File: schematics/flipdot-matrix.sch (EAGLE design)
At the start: 42 parts

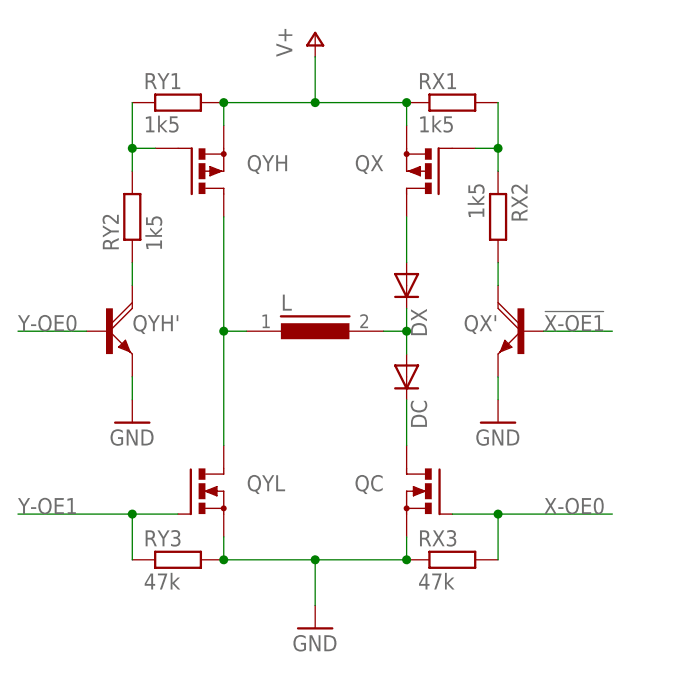
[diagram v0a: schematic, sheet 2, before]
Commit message: updated matrix schematics
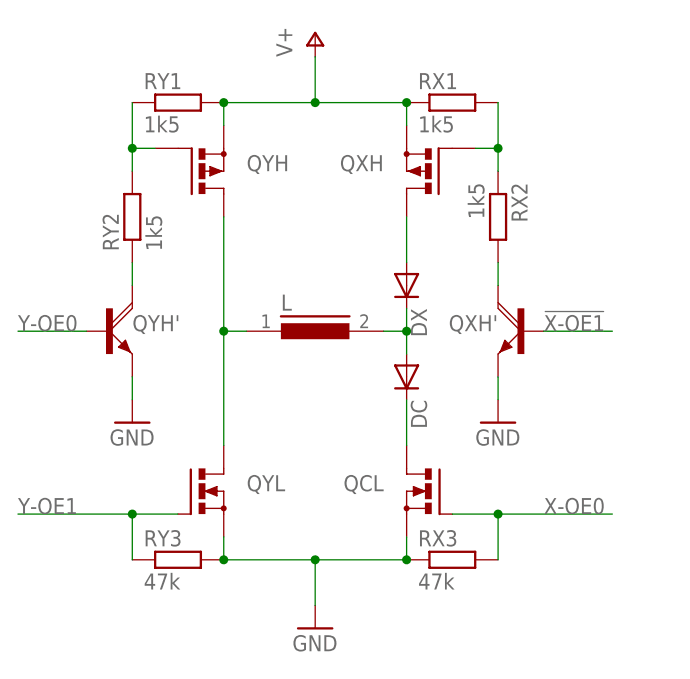
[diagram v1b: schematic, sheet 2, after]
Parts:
- renumbered QC to QCL, QX to QXH, QX' to QXH'
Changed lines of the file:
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@@
 <part name="L" library="inductors" deviceset="DS10" device="" value=""/>
 <part name="QYH" library="transistor-power" deviceset="PMOSFET_P" device="TO220BV"/>
-<part name="QX" library="transistor-power" deviceset="PMOSFET_P" device="TO220BV"/>
+<part name="QXH" library="transistor-power" deviceset="PMOSFET_P" device="TO220BV"/>
 <part name="QYL" library="transistor-power" deviceset="PMOSFET_N" device="TO220BV"/>
-<part name="QC" library="transistor-power" deviceset="PMOSFET_N" device="TO220BV"/>
+<part name="QCL" library="transistor-power" deviceset="PMOSFET_N" device="TO220BV"/>
 <part name="DC" library="diode" deviceset="1N4004" device="" value=""/>
 <part name="DX" library="diode" deviceset="1N4004" device="" value=""/>
@@
 <part name="P+2" library="supply1" deviceset="V+" device=""/>
 <part name="QYH'" library="transistor-power" deviceset="BD679" device="" value=""/>
-<part name="QX'" library="transistor-power" deviceset="BD679" device="" value=""/>
+<part name="QXH'" library="transistor-power" deviceset="BD679" device="" value=""/>
 <part name="GND1" library="supply1" deviceset="GND" device=""/>
 <part name="GND3" library="supply1" deviceset="GND" device=""/>
@@
 <sheets>
 <sheet>
-<description>Flip Dot Matrix</description>
+<description>Matrix</description>
 <plain>
 <rectangle x1="7.62" y1="50.8" x2="27.94" y2="71.12" layer="97"/>
@@
 </sheet>
 <sheet>
-<description>Flip Dot Pixel</description>
+<description>Pixel</description>
 <plain>
 </plain>
@@
 <attribute name="VALUE" x="25.4" y="53.34" size="1.778" layer="96"/>
 </instance>
-<instance part="QX" gate="G$1" x="45.72" y="53.34" smashed="yes" rot="MR0">
+<instance part="QXH" gate="G$1" x="45.72" y="53.34" smashed="yes" rot="MR0">
 <attribute name="NAME" x="40.64" y="53.34" size="1.778" layer="95" rot="MR0"/>
 <attribute name="VALUE" x="40.64" y="53.34" size="1.778" layer="96" rot="MR0"/>
@@
 <attribute name="VALUE" x="25.4" y="17.78" size="1.778" layer="96"/>
 </instance>
-<instance part="QC" gate="G$1" x="45.72" y="17.78" smashed="yes" rot="MR0">
+<instance part="QCL" gate="G$1" x="45.72" y="17.78" smashed="yes" rot="MR0">
 <attribute name="NAME" x="40.64" y="17.78" size="1.778" layer="95" rot="MR0"/>
 <attribute name="VALUE" x="40.64" y="17.78" size="1.778" layer="96" rot="MR0"/>
@@
 <attribute name="VALUE" x="15.24" y="35.56" size="1.778" layer="96"/>
 </instance>
-<instance part="QX'" gate="1" x="55.88" y="35.56" smashed="yes" rot="MR0">
+<instance part="QXH'" gate="1" x="55.88" y="35.56" smashed="yes" rot="MR0">
 <attribute name="NAME" x="53.34" y="35.56" size="1.778" layer="95" rot="MR0"/>
 <attribute name="VALUE" x="50.8" y="35.56" size="1.778" layer="96" rot="MR0"/>
@@
 <net name="N$24" class="0">
 <segment>
-<pinref part="QX" gate="G$1" pin="D"/>
+<pinref part="QXH" gate="G$1" pin="D"/>
 <pinref part="DX" gate="1" pin="A"/>
 <wire x1="43.18" y1="48.26" x2="43.18" y2="43.18" width="0.1524" layer="91"/>
@@
 <net name="N$26" class="0">
 <segment>
-<pinref part="QC" gate="G$1" pin="D"/>
+<pinref part="QCL" gate="G$1" pin="D"/>
 <pinref part="DC" gate="1" pin="C"/>
 <wire x1="43.18" y1="22.86" x2="43.18" y2="27.94" width="0.1524" layer="91"/>
@@
 <net name="X-OE0" class="0">
 <segment>
-<pinref part="QC" gate="G$1" pin="G"/>
+<pinref part="QCL" gate="G$1" pin="G"/>
 <wire x1="48.26" y1="15.24" x2="53.34" y2="15.24" width="0.1524" layer="91"/>
 <label x="58.42" y="15.24" size="1.778" layer="95"/>
@@
 <junction x="22.86" y="60.96"/>
 <pinref part="RX1" gate="G$1" pin="1"/>
-<pinref part="QX" gate="G$1" pin="S"/>
+<pinref part="QXH" gate="G$1" pin="S"/>
 <wire x1="43.18" y1="60.96" x2="43.18" y2="58.42" width="0.1524" layer="91"/>
 <junction x="43.18" y="60.96"/>
@@
 <wire x1="43.18" y1="10.16" x2="33.02" y2="10.16" width="0.1524" layer="91"/>
 <junction x="33.02" y="10.16"/>
-<pinref part="QC" gate="G$1" pin="S"/>
+<pinref part="QCL" gate="G$1" pin="S"/>
 <wire x1="43.18" y1="12.7" x2="43.18" y2="10.16" width="0.1524" layer="91"/>
 <junction x="43.18" y="10.16"/>
@@
 <segment>
 <pinref part="GND3" gate="1" pin="GND"/>
-<pinref part="QX'" gate="1" pin="E"/>
+<pinref part="QXH'" gate="1" pin="E"/>
 <wire x1="53.34" y1="30.48" x2="53.34" y2="27.94" width="0.1524" layer="91"/>
 </segment>
@@
 <net name="!X-OE1" class="0">
 <segment>
-<pinref part="QX'" gate="1" pin="B"/>
+<pinref part="QXH'" gate="1" pin="B"/>
 <wire x1="58.42" y1="35.56" x2="66.04" y2="35.56" width="0.1524" layer="91"/>
 <label x="58.42" y="35.56" size="1.778" layer="95"/>
@@
 <net name="N$11" class="0">
 <segment>
-<pinref part="QX'" gate="1" pin="C"/>
+<pinref part="QXH'" gate="1" pin="C"/>
 <pinref part="RX2" gate="G$1" pin="2"/>
 <wire x1="53.34" y1="40.64" x2="53.34" y2="43.18" width="0.1524" layer="91"/>
@@
 <pinref part="RX1" gate="G$1" pin="2"/>
 <wire x1="53.34" y1="53.34" x2="53.34" y2="55.88" width="0.1524" layer="91"/>
-<pinref part="QX" gate="G$1" pin="G"/>
+<pinref part="QXH" gate="G$1" pin="G"/>
 <wire x1="53.34" y1="55.88" x2="53.34" y2="60.96" width="0.1524" layer="91"/>
 <wire x1="50.8" y1="55.88" x2="53.34" y2="55.88" width="0.1524" layer="91"/>

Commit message: updated flipdot pixel: X-OE0 is inverted, not X-OE1
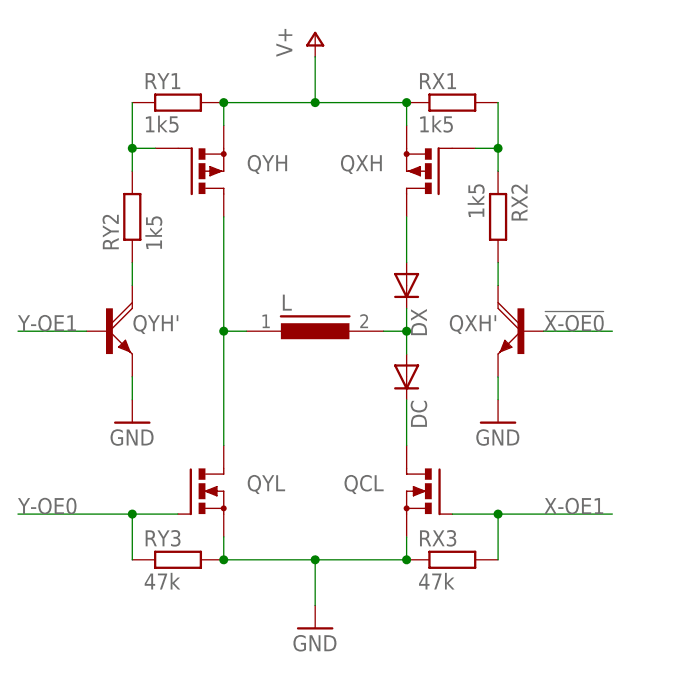
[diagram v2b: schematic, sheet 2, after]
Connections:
- net !X-OE1 renamed !X-OE0
- net X-OE0 renamed X-OE1
- net Y-OE0: now also QYL.G, RY3.1; no longer QYH'.B
- net Y-OE1: now also QYH'.B; no longer QYL.G, RY3.1
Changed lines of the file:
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@@
 </segment>
 </net>
-<net name="X-OE0" class="0">
+<net name="X-OE1" class="0">
 <segment>
 <pinref part="QCL" gate="G$1" pin="G"/>
@@
 </segment>
 </net>
-<net name="Y-OE1" class="0">
+<net name="Y-OE0" class="0">
 <segment>
 <pinref part="QYL" gate="G$1" pin="G"/>
@@
 </segment>
 </net>
-<net name="Y-OE0" class="0">
+<net name="Y-OE1" class="0">
 <segment>
 <pinref part="QYH'" gate="1" pin="B"/>
@@
 </segment>
 </net>
-<net name="!X-OE1" class="0">
+<net name="!X-OE0" class="0">
 <segment>
 <pinref part="QXH'" gate="1" pin="B"/>
